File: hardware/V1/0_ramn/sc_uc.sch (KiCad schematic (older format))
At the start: 20 parts, among them J6 , U10 ATA6561-GAQW-N, U11 STM32L443CCTx, Y4 NX3225GD-8MHZ-STD-CRA-3

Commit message: Added initial V1 Firmware and Scripts
- Minor hardware fixes
- Minor documentation fixes
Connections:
- net CAN_STB: now also U11.3 (PC14); no longer U11.30 (PA9)
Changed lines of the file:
@@
 Sheet 8 9
 Title "RAMN: Resistant Automotive Miniature Network V1.0"
-Date "2021-02-20"
-Rev "A"
+Date "2021-06-01"
+Rev "B2L"
 Comp "Copyright (c) 2021 TOYOTA MOTOR CORPORATION. ALL RIGHTS RESERVED."
 Comment1 ""
@@
 Wire Wire Line
 	8450 3650 8400 3650
-Text Label 9800 4950 0    50   ~ 0
+Text Label 8300 3750 2    50   ~ 0
 CAN_STB
 Wire Wire Line
@@
 Wire Wire Line
 	6400 3350 6400 3450
-NoConn ~ 8450 3750
 NoConn ~ 8450 3850
 $Sheet
@@
 Text HLabel 8150 3450 0    50   Input ~ 0
 BOOT0
-Wire Wire Line
-	9800 4950 9650 4950
 $Comp
 L Device:R_Small_US R?
@@
 Wire Wire Line
 	9250 2750 9250 2850
+Wire Wire Line
+	8450 3750 8300 3750
+NoConn ~ 9650 4950
 $EndSCHEMATC

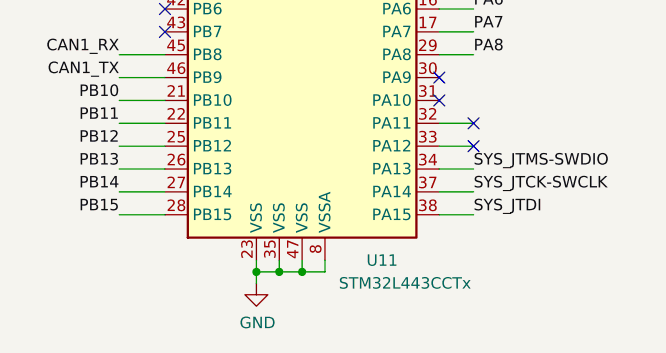
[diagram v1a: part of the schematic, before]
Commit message: Updated schematics to show BOOT0 resistor settings for STM32L5 microcontrollers
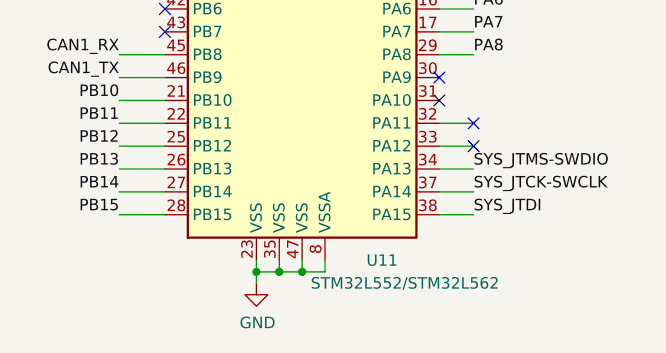
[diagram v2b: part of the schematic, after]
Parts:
- U11: value STM32L443CCTx -> STM32L552/STM32L562
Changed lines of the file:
@@
 Sheet 8 9
 Title "RAMN: Resistant Automotive Miniature Network V1.0"
-Date "2021-06-01"
+Date "2024-02-20"
 Rev "B2L"
-Comp "Copyright (c) 2021 TOYOTA MOTOR CORPORATION. ALL RIGHTS RESERVED."
+Comp "Copyright (c) 2024 TOYOTA MOTOR CORPORATION. ALL RIGHTS RESERVED."
 Comment1 ""
 Comment2 ""
@@
 AR Path="/5D7DEA89/5D7F2860" Ref="U11"  Part="1"
 F 0 "U11" H 9400 2750 50  0000 C CNN
-F 1 "STM32L443CCTx" H 9500 2650 50  0000 C CNN
+F 1 "STM32L552/STM32L562" H 9500 2650 50  0000 C CNN
 F 2 "Package_QFP:LQFP-48_7x7mm_P0.5mm" H 8550 2850 50  0001 R CNN
 F 3 "http://www.st.com/st-web-ui/static/active/en/resource/technical/document/datasheet/DM00254865.pdf" H 9050 4250 50  0001 C CNN
